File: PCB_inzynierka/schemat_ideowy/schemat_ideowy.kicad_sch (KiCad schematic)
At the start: 13 parts, among them J1 Barrel_Jack_Switch, SW73 SW_DPST, SW74 SW_DPST, SW75 SW_DPST, SW76 SW_DPST, U10 TFT_320x240, U11 NUCLEO-F401RE

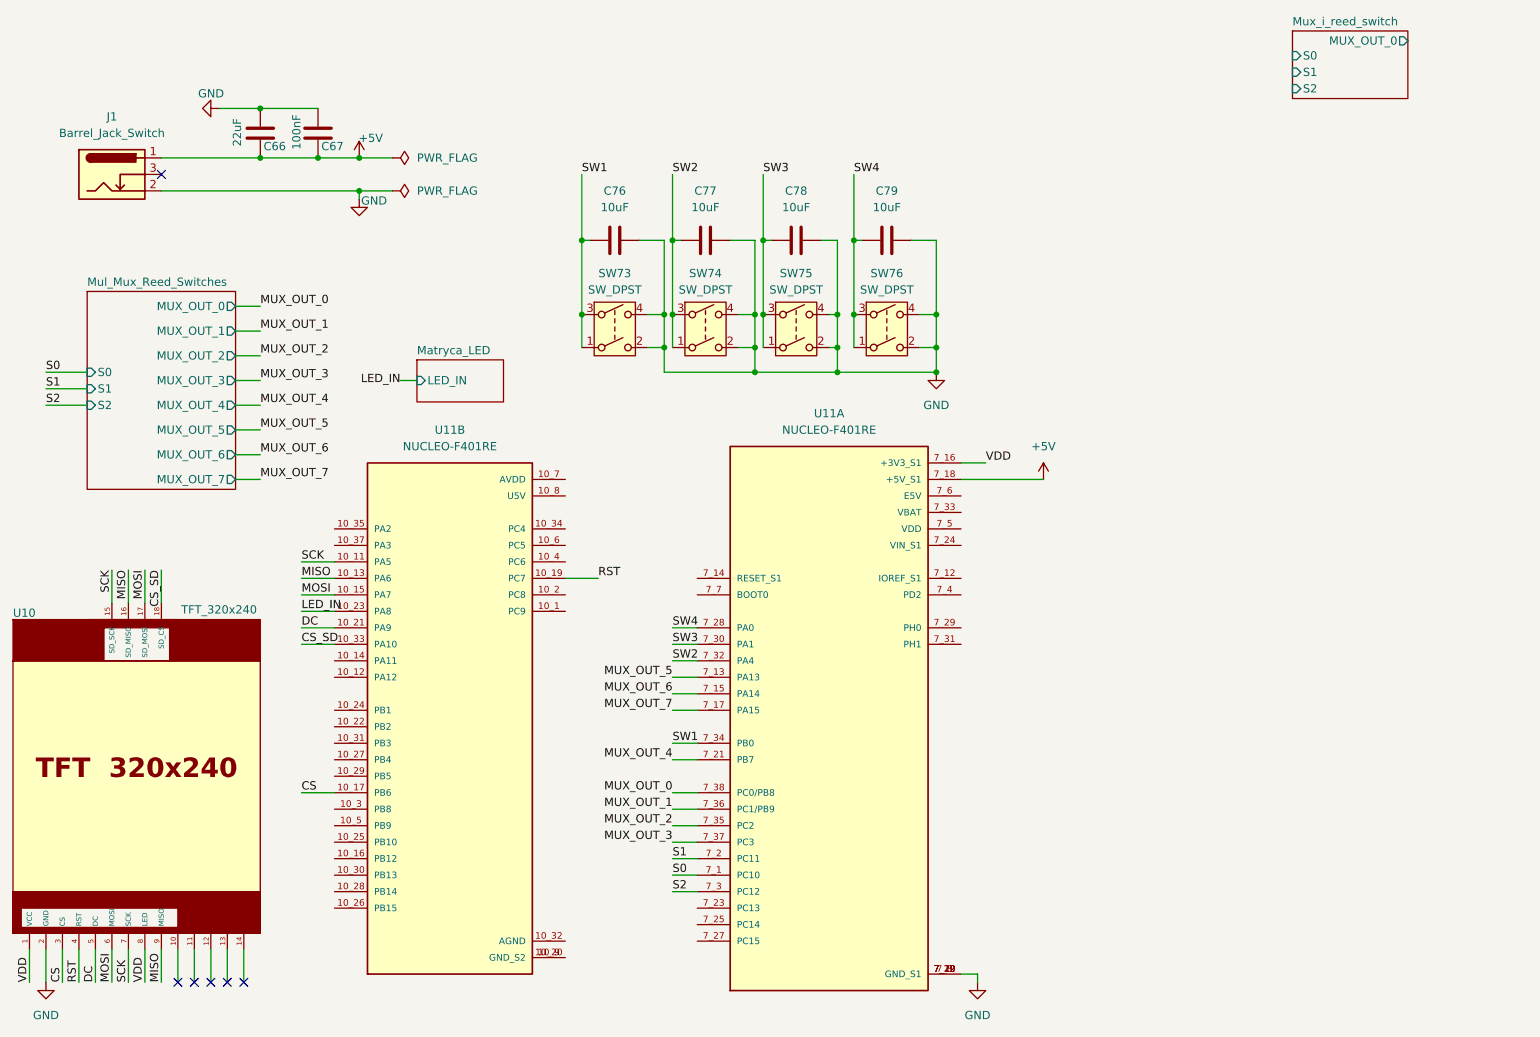
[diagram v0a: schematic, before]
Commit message: obie plytki pcb przygotowane, schematy ideowe opisane
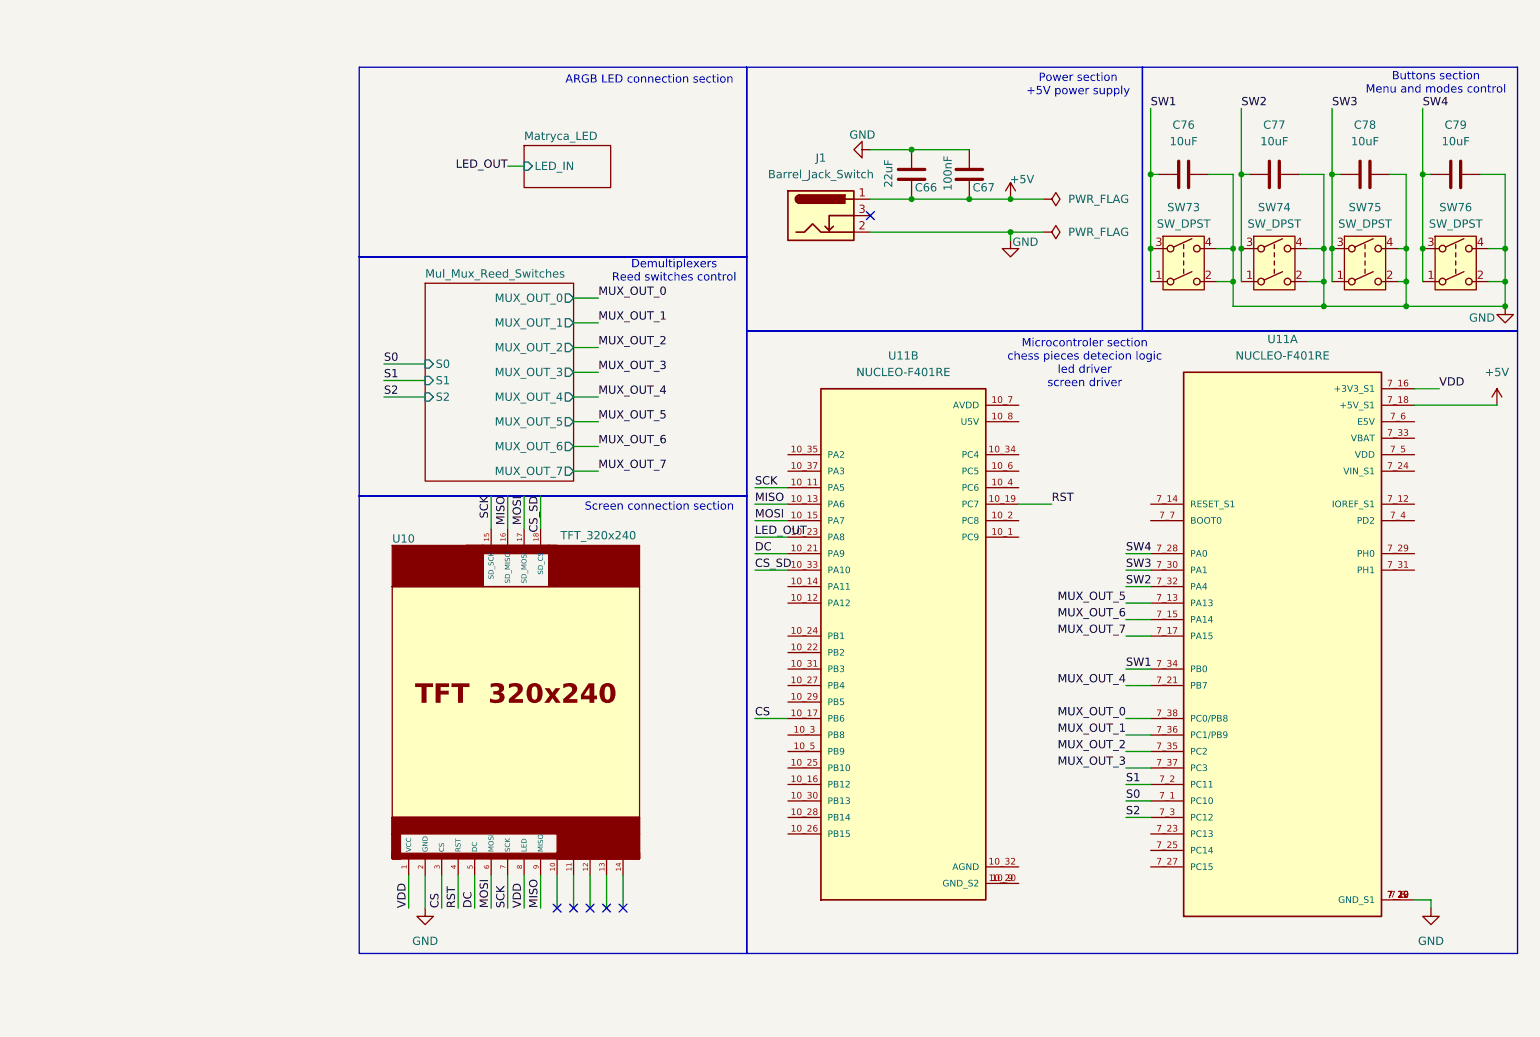
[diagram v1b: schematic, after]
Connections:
- net LED_IN renamed LED_OUT
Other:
- removed sheet Mux_i_reed_switch
- note added: "ARGB LED connection section"
- note added: "Buttons section Menu and modes control"
- note added: "Demultiplexers Reed switches control"
- note added: "Microcontroler section chess pieces detecion logic led driver screen driver"
- note added: "Power section +5V power supply"
- note added: "Screen connection section"
- company: (none) -> AGH
- title: (none) -> Schemat ideowy całego projektu
- moved on the sheet: C66, C67, C76, C77, C78, C79, J1, SW73, SW74, SW75, SW76, U10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
